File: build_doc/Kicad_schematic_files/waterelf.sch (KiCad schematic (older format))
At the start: 1 part

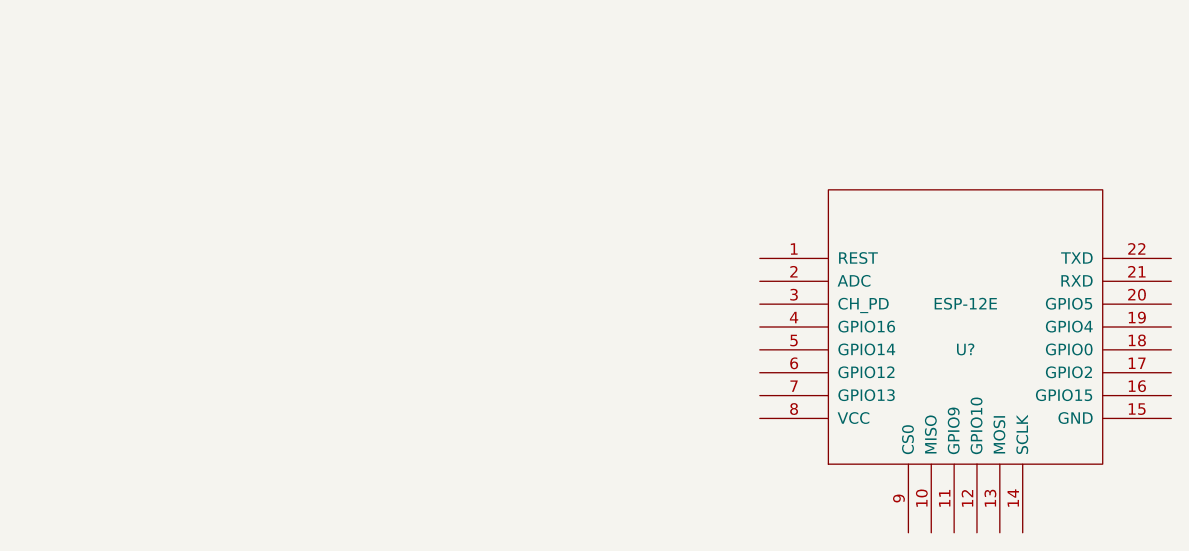
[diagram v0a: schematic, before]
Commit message: updated libraries, got newPing library implementation started
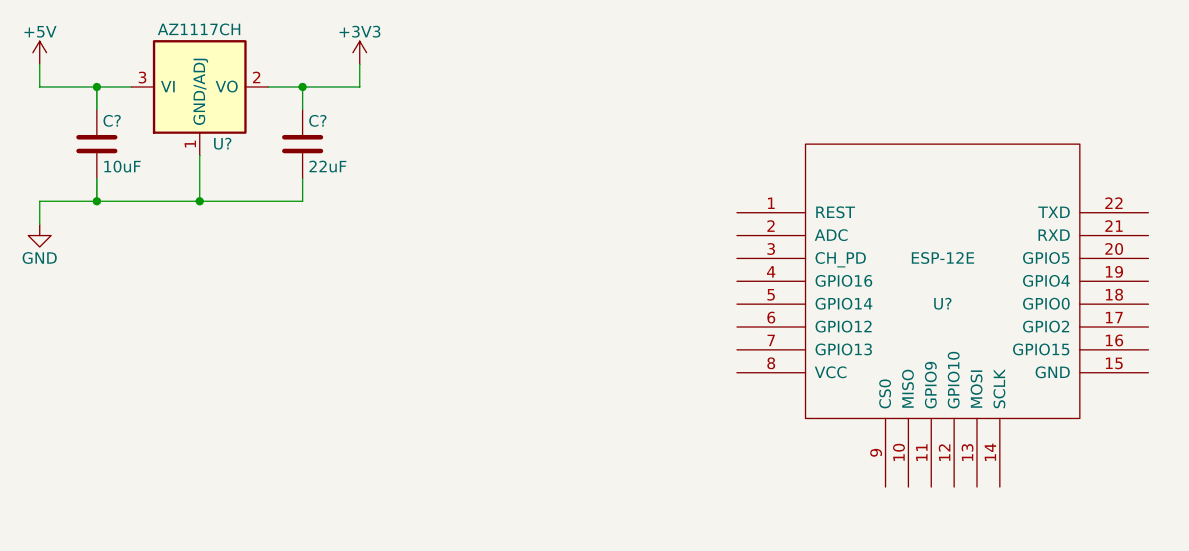
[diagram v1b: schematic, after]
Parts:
- added C?: 10uF, symbol C
- added C?: 22uF, symbol C
- added U?: AZ1117CH, SOT223, symbol AZ1117CH
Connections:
- new net +3V3: C?.1, U?.2 (VO)
- new net +5V: C?.1, U?.3 (VI)
- new net GND: C?.2, C?.2, U?.1 (GND/ADJ)
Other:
- moved on the sheet: U?
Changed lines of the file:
@@
-EESchema Schematic File Version 2  date Thu 02 Jun 2016 09:24:40 BST
+EESchema Schematic File Version 2
 LIBS:power
 LIBS:device
@@
 LIBS:ESP8266
 LIBS:waterelf
-EELAYER 25  0
+LIBS:waterelf-cache
+EELAYER 25 0
 EELAYER END
-$Descr A4 11700 8267
+$Descr A4 11693 8268
 encoding utf-8
 Sheet 1 1
@@
 L ESP-12E U?
 U 1 1 574FED3F
-P 5250 2450
-F 0 "U?" H 5250 2350 50  0000 C CNN
-F 1 "ESP-12E" H 5250 2550 50  0000 C CNN
-	1    5250 2450
+P 5150 2250
+F 0 "U?" H 5150 2150 50  0000 C CNN
+F 1 "ESP-12E" H 5150 2350 50  0000 C CNN
+F 2 "" H 5150 2250 60  0001 C CNN
+F 3 "" H 5150 2250 60  0001 C CNN
+	1    5150 2250
 	1    0    0    -1
 $EndComp
+$Comp
+L +5V #PWR?
+U 1 1 575438F9
+P 1200 1300
+F 0 "#PWR?" H 1200 1150 50  0001 C CNN
+F 1 "+5V" H 1200 1440 50  0000 C CNN
+F 2 "" H 1200 1300 50  0000 C CNN
+F 3 "" H 1200 1300 50  0000 C CNN
+	1    1200 1300
+	1    0    0    -1
+$EndComp
+$Comp
+L C C?
+U 1 1 57543D01
+P 1450 1650
+F 0 "C?" H 1475 1750 50  0000 L CNN
+F 1 "10uF" H 1475 1550 50  0000 L CNN
+F 2 "" H 1488 1500 50  0000 C CNN
+F 3 "" H 1450 1650 50  0000 C CNN
+	1    1450 1650
+	1    0    0    -1
+$EndComp
+$Comp
+L C C?
+U 1 1 57543D6A
+P 2350 1650
+F 0 "C?" H 2375 1750 50  0000 L CNN
+F 1 "22uF" H 2375 1550 50  0000 L CNN
+F 2 "" H 2388 1500 50  0000 C CNN
+F 3 "" H 2350 1650 50  0000 C CNN
+	1    2350 1650
+	1    0    0    -1
+$EndComp
+Connection ~ 2350 1400
+Wire Wire Line
+	1450 1400 1450 1500
+Connection ~ 1450 1400
+$Comp
+L GND #PWR?
+U 1 1 5754435F
+P 1200 2000
+F 0 "#PWR?" H 1200 1750 50  0001 C CNN
+F 1 "GND" H 1200 1850 50  0000 C CNN
+F 2 "" H 1200 2000 50  0000 C CNN
+F 3 "" H 1200 2000 50  0000 C CNN
+	1    1200 2000
+	1    0    0    -1
+$EndComp
+Wire Wire Line
+	1900 1700 1900 1900
+$Comp
+L +3V3 #PWR?
+U 1 1 5754456B
+P 2600 1300
+F 0 "#PWR?" H 2600 1150 50  0001 C CNN
+F 1 "+3V3" H 2600 1440 50  0000 C CNN
+F 2 "" H 2600 1300 50  0000 C CNN
+F 3 "" H 2600 1300 50  0000 C CNN
+	1    2600 1300
+	1    0    0    -1
+$EndComp
+Wire Wire Line
+	2600 1400 2600 1300
+$Comp
+L AZ1117CH U?
+U 1 1 575442BE
+P 1900 1400
+F 0 "U?" H 2000 1150 50  0000 C CNN
+F 1 "AZ1117CH" H 1900 1650 50  0000 C CNN
+F 2 "SOT223" H 1900 1050 50  0001 C CNN
+F 3 "http://www.diodes.com/_files/datasheets/AZ1117C.pdf" H 2000 1150 50  0001 C CNN
+	1    1900 1400
+	1    0    0    -1
+$EndComp
+Wire Wire Line
+	2350 1500 2350 1400
+Wire Wire Line
+	1200 1900 1200 2000
+Wire Wire Line
+	1200 1400 1200 1300
+Wire Wire Line
+	2200 1400 2600 1400
+Wire Wire Line
+	1200 1400 1600 1400
+Wire Wire Line
+	1200 1900 2350 1900
+Wire Wire Line
+	2350 1900 2350 1800
+Connection ~ 1900 1900
+Wire Wire Line
+	1450 1800 1450 1900
+Connection ~ 1450 1900
 $EndSCHEMATC

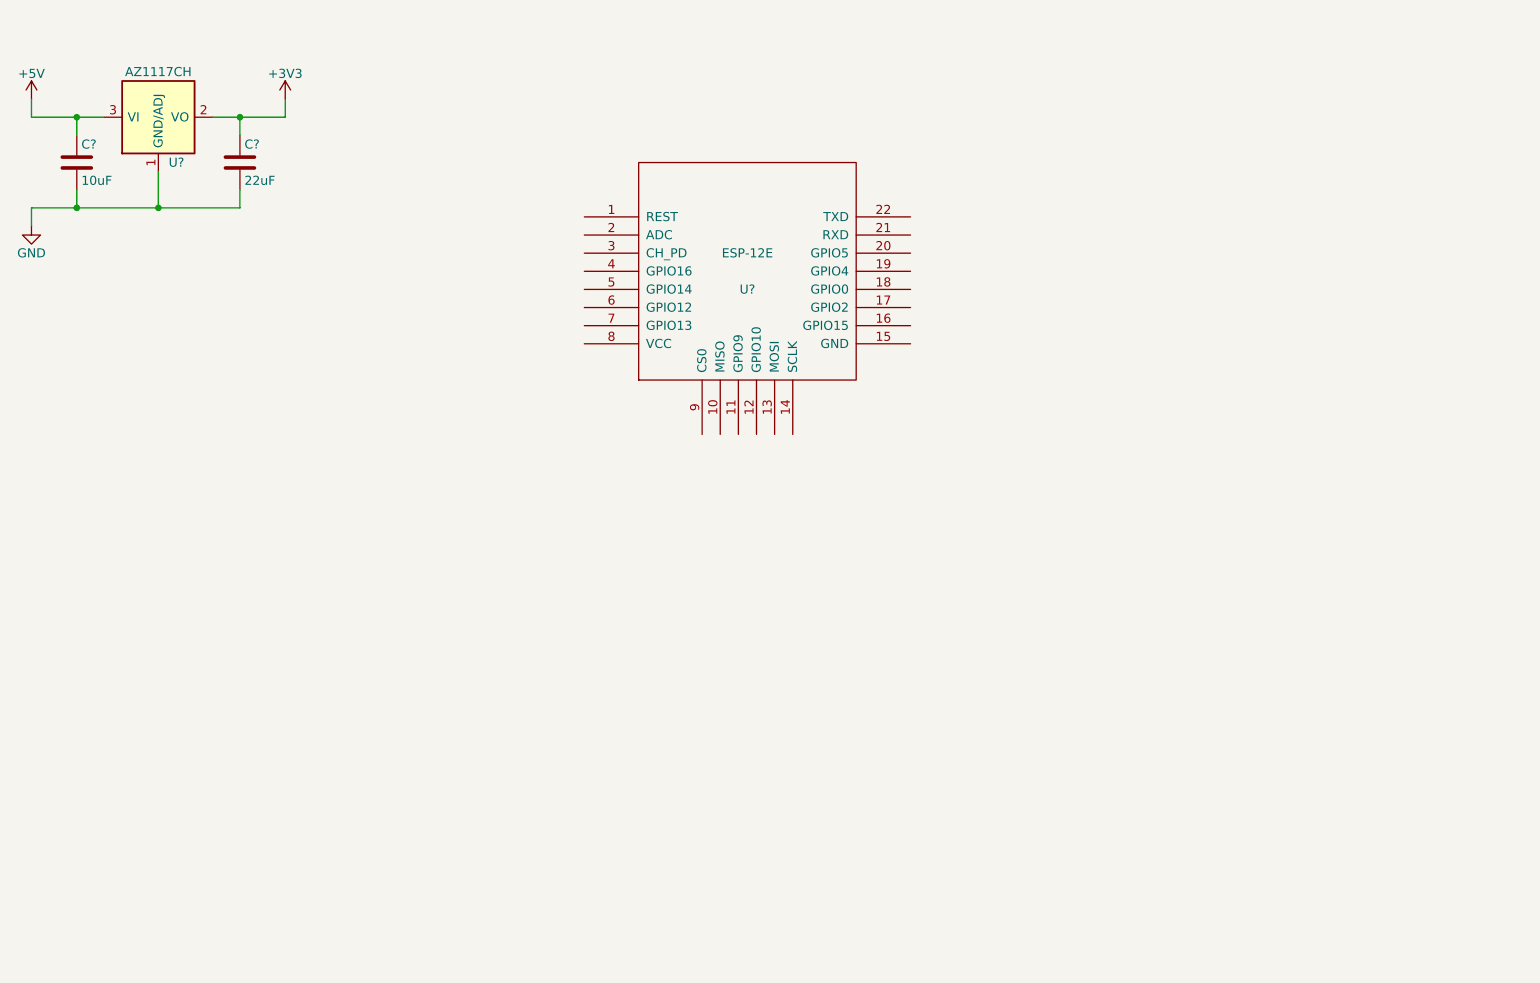
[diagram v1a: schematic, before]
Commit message: tweaked schematic, updated BOM with uk ebay links
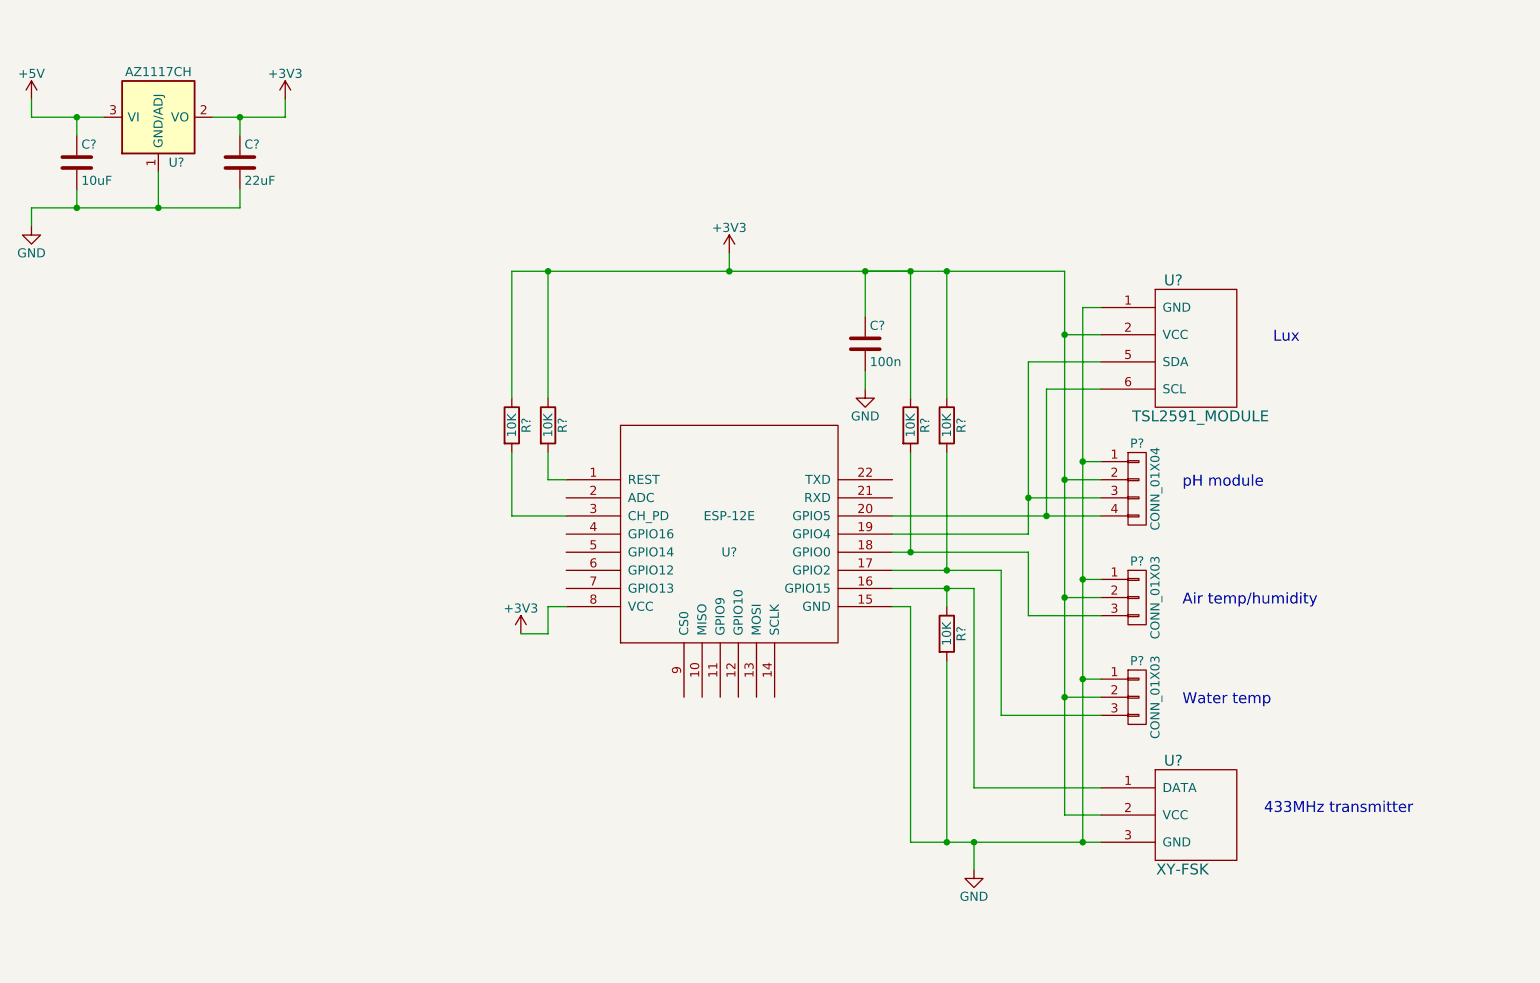
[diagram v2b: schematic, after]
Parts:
- added C?: 100n, symbol C
- added P?: CONN_01X04, symbol CONN_01X04
- added P? (x2): CONN_01X03, symbol CONN_01X03
- added R? (x5): 10K, symbol R
- added U?: TSL2591_MODULE, symbol TSL2591_MODULE
- added U?: XY-FSK, symbol XY-FSK
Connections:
- net +3V3: now also U?.8 (VCC), C?.1, P?.2 (P2), P?.2 (P2), P?.2 (P2), R?.1, R?.1, R?.1, R?.1, U?.2 (VCC), U?.2 (VCC)
- net GND: now also U?.15 (GND), C?.2, P?.1 (P1), P?.1 (P1), P?.1 (P1), R?.2, U?.1 (GND), U?.3 (GND)
- net at U?.1 (REST): now also R?.2
- net at U?.16 (GPIO15): now also R?.1, U?.1 (DATA)
- net at U?.17 (GPIO2): now also P?.3 (P3), R?.2
- net at U?.18 (GPIO0): now also P?.3 (P3), R?.2
- net at U?.19 (GPIO4): now also P?.3 (P3), U?.5 (SDA)
- net at U?.20 (GPIO5): now also P?.4 (P4), U?.6 (SCL)
- net at U?.3 (CH_PD): now also R?.2
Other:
- note added: "433MHz transmitter"
- note added: "Air temp/humidity"
- note added: "Lux"
- note added: "Water temp"
- note added: "pH module"
- moved on the sheet: U?

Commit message: added dashboard flow
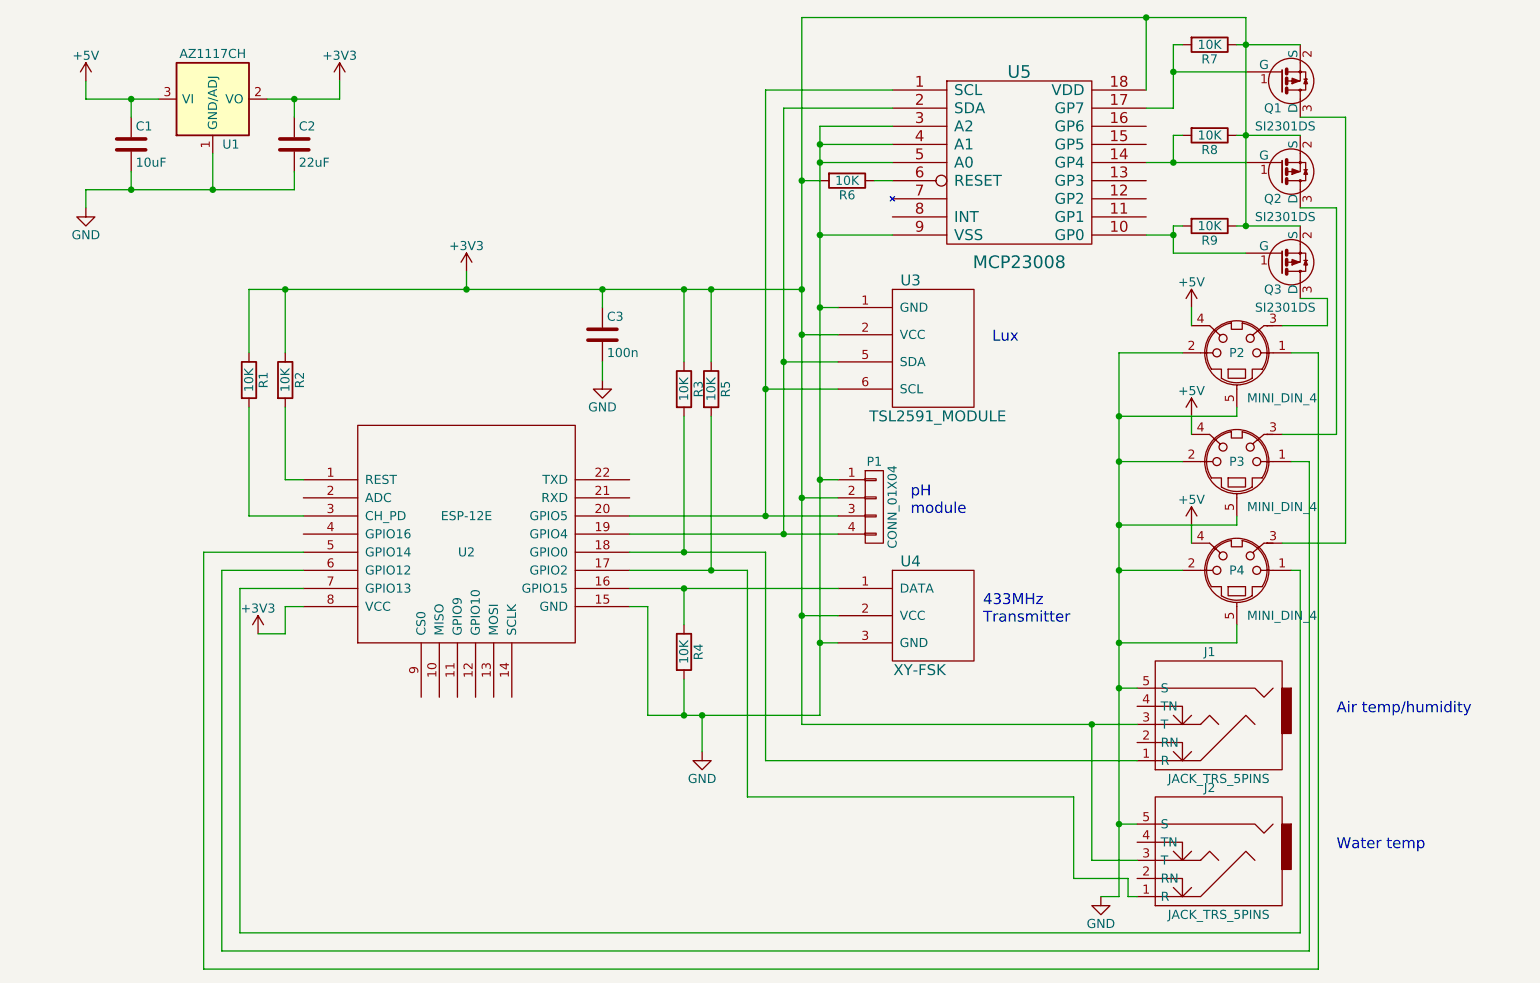
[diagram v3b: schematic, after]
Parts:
- removed P? (x2): CONN_01X03, symbol CONN_01X03
- added J1, J2: JACK_TRS_5PINS, symbol JACK_TRS_5PINS
- added P2, P3, P4: MINI_DIN_4, symbol MINI_DIN_4
- added Q1, Q2, Q3: SI2301DS, SOT-23, symbol SI2301DS
- added R6, R7, R8, R9: 10K, symbol R
- added U5: MCP23008, symbol MCP23008
- gave numbers to parts that had none: 13
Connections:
- net +3V3: now also J1.3 (T), J2.3 (T), Q1.2 (S), Q2.2 (S), Q3.2 (S), R6.2, R7.1, R8.1, R9.1, U5.18 (VDD)
- net +5V: now also P2.4, P3.4, P4.4
- net GND: now also J1.5 (S), J2.5 (S), P2.2, P2.5 (SHEILD), P3.2, P3.5 (SHEILD), P4.2, P4.5 (SHEILD), U5.3 (A2), U5.4 (A1), U5.5 (A0), U5.9 (VSS)
- net at R5.2, U2.17 (GPIO2): now also J2.1 (R)
- net at R3.2, U2.18 (GPIO0): now also J1.1 (R)
- net at U2.19 (GPIO4), U3.5 (SDA): now also P1.4 (P4), U5.2 (SDA); no longer P1.3 (P3)
- net at U2.20 (GPIO5), U3.6 (SCL): now also P1.3 (P3), U5.1 (SCL); no longer P1.4 (P4)
- net at U2.5 (GPIO14): now also P2.1
- net at U2.6 (GPIO12): now also P3.1
- net at U2.7 (GPIO13): now also P4.1
- new net: Q3.1 (G), R9.2, U5.10 (GP0)
- new net: Q2.1 (G), R8.2, U5.14 (GP4)
- new net: Q1.1 (G), R7.2, U5.17 (GP7)
- new net: R6.1, U5.6 (RESET)
- new net: P2.3, Q3.3 (D)
- new net: P4.3, Q1.3 (D)
- new net: P3.3, Q2.3 (D)
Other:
- note added: "433MHz\nTransmitter"
- note added: "pH\nmodule"
- note removed: "433MHz transmitter"
- note removed: "pH module"
- moved on the sheet: C1, C2, C3, P1, R1, R2, R3, R4, R5, U1, U2, U3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
